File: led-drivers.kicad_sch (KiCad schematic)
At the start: 37 parts, among them U5 TLC5971PWP, U6 TLC5971PWP, U7 LIS2DH

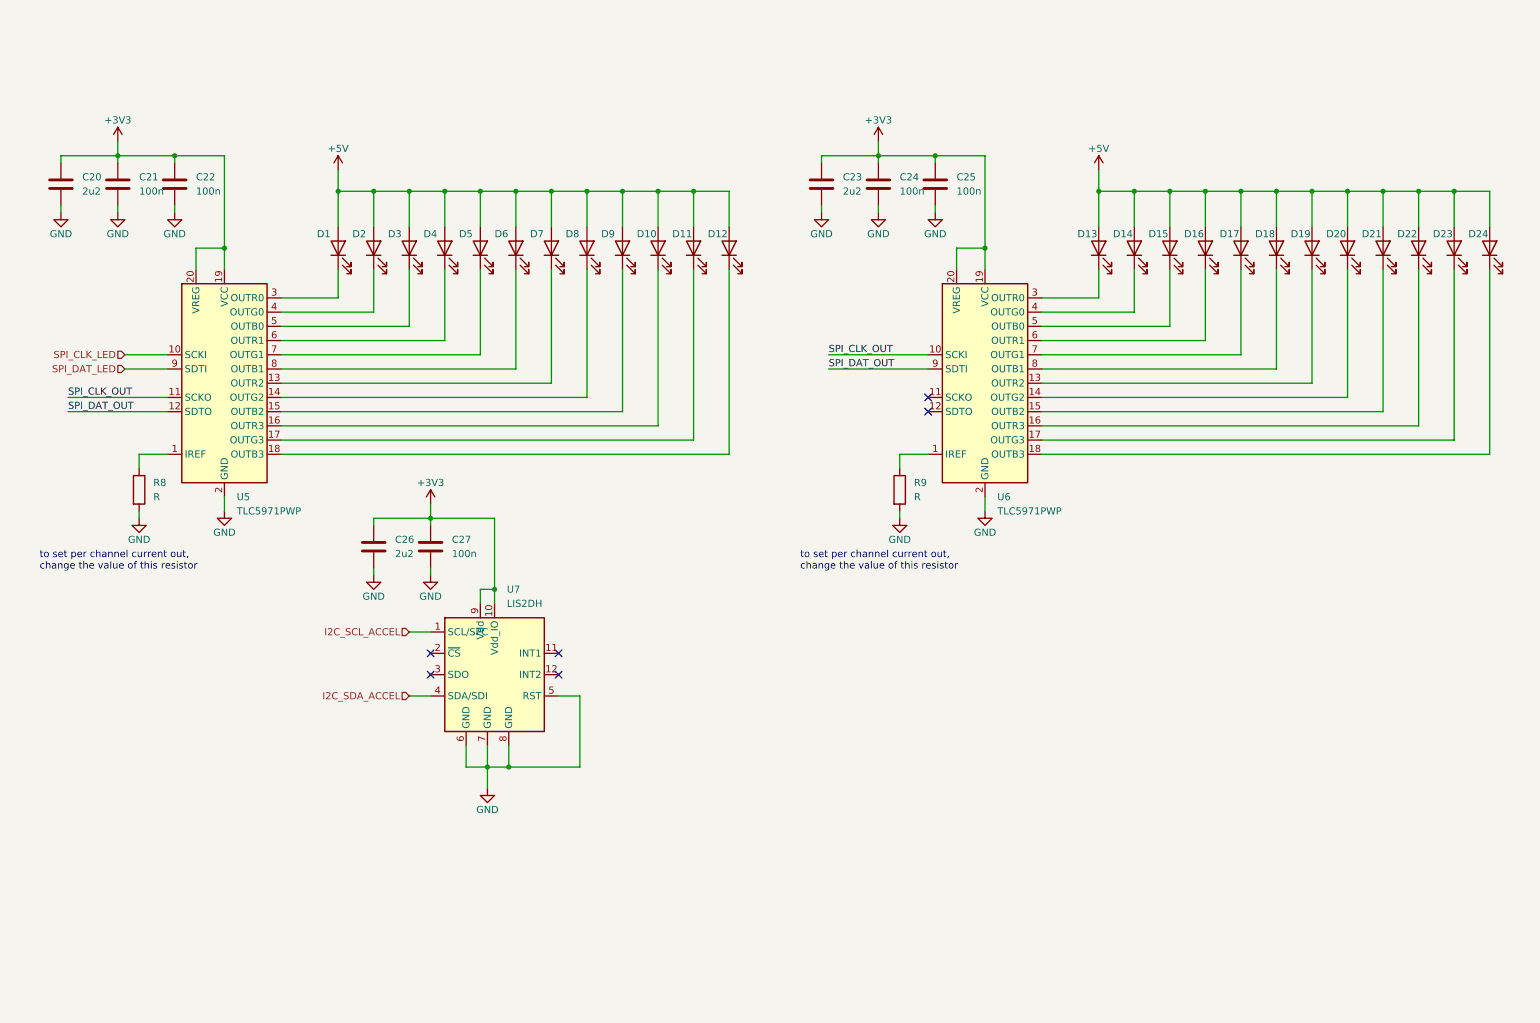
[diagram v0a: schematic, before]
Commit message: Added part numbers, footprints and improved formatting
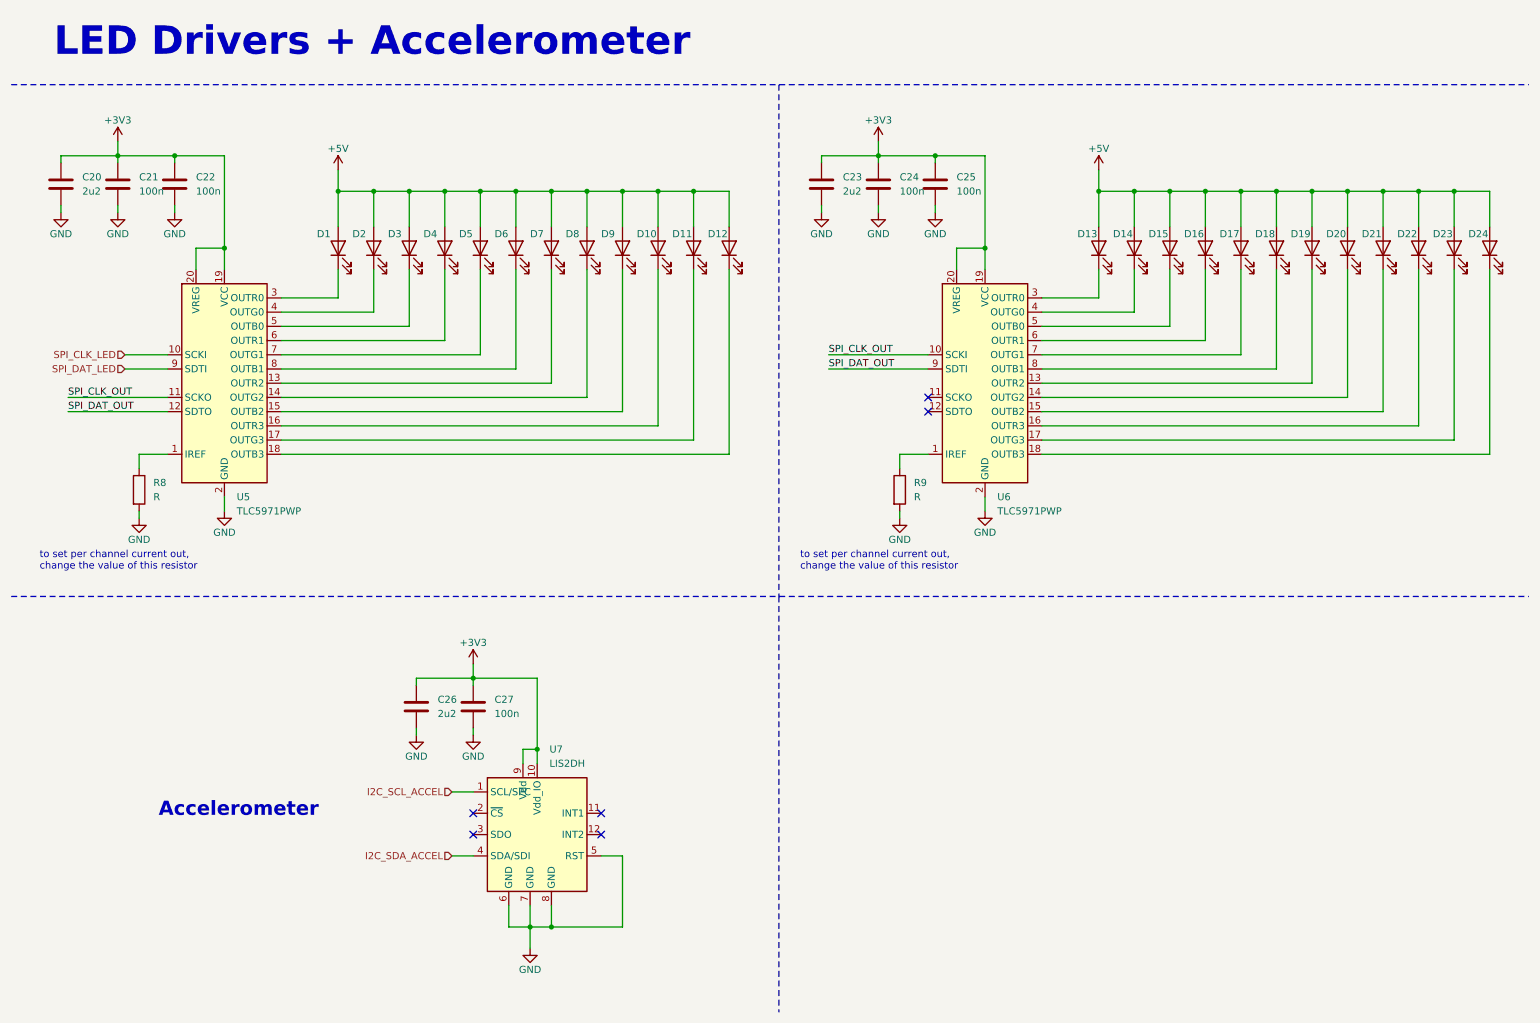
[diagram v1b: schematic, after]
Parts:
- C20, C23, C26: footprint (none) -> Capacitor_SMD:C_0805_2012Metric; symbol Device:C -> jellybeans:C-0805-2u2-25V; JLC (none) -> C377773; MFG (none) -> Samsung Electro-Mechanics; MPN (none) -> CL21A225KBQNNNE
- C21, C22, C24, C25, C27: footprint (none) -> Capacitor_SMD:C_0603_1608Metric; symbol Device:C -> jellybeans:C-0603-100n-50V; JLC (none) -> C14663; MFG (none) -> YAGEO; MPN (none) -> CC0603KRX7R9BB104
- D1, D2, D3: footprint (none) -> LED_SMD:LED_0805_2012Metric
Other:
- note added: "Accelerometer"
- note added: "LED Drivers + Accelerometer"
- title: (none) -> Pico + LEDs
- moved on the sheet: C26, C27, U7
